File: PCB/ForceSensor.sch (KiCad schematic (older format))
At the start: 12 parts, among them J1 Conn_01x15, J2 Conn_01x15, J3 Conn_01x02, J4 Conn_01x01, J5 Conn_01x01, U1 MCP6004, U2 L7905

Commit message: New schematic
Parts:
- removed A1: Arduino_Nano_v3.x, Module:Arduino_Nano, symbol MCU_Module:Arduino_Nano_v3.x
- removed C1: C_Small, symbol Device:C_Small
- removed J1, J2: Conn_01x15, symbol Connector_Generic:Conn_01x15
- removed J3: Conn_01x02, symbol Connector_Generic:Conn_01x02
- removed J4, J5: Conn_01x01, symbol Connector_Generic:Conn_01x01
- removed R1, R2, R3: R, symbol Device:R
- removed U1: MCP6004, symbol Amplifier_Operational:MCP6004
- removed U2: L7905, symbol Regulator_Linear:L7905
- added C? (x6): C_Small, symbol Device:C_Small
- added J? (x2): Conn_01x10, symbol Connector_Generic:Conn_01x10
- added R? (x8): R_Small_US, symbol Device:R_Small_US
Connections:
- net labels removed: +3V, +5V, -5V, GND, VIN
- wire segments 36 -> 0
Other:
- note removed: "-5V regulator"
- note removed: "-Vref for sensors\n(Step down to 1V)"
- note removed: "Amplify Sensor Signal"
- note removed: "Connectors for Arduino"
- note removed: "Power from Battery to Arduino"
- note removed: "Power the OpAmps"
- note removed: "Sensor"
- note removed: "To sensors"

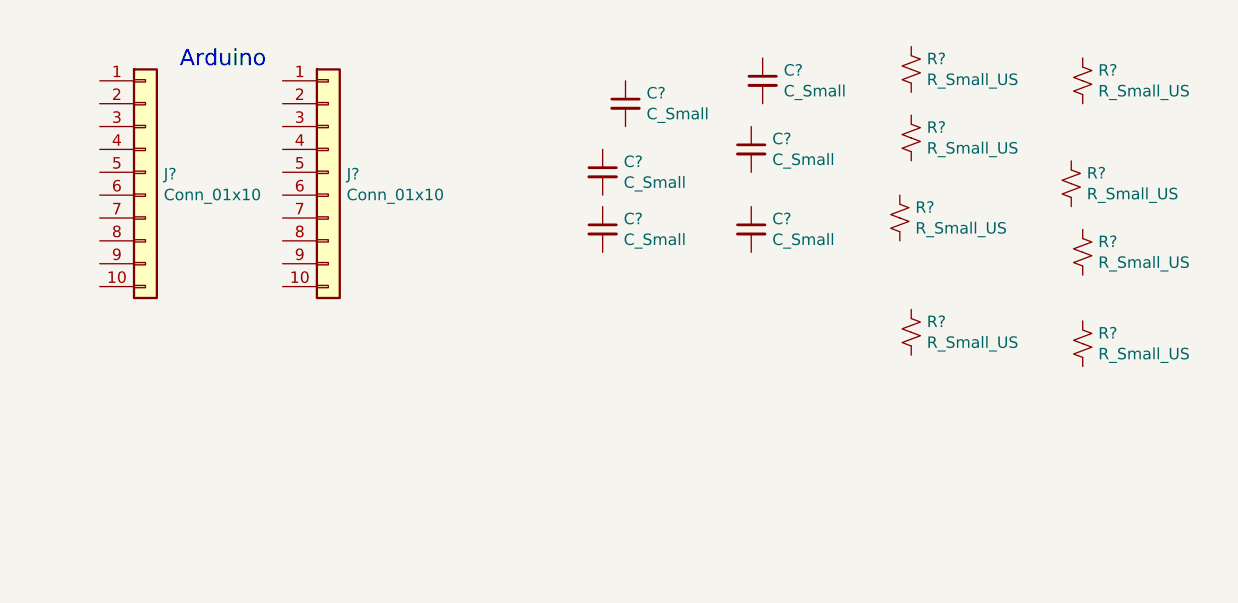
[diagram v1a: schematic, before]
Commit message: Added schematics for rfs pcb
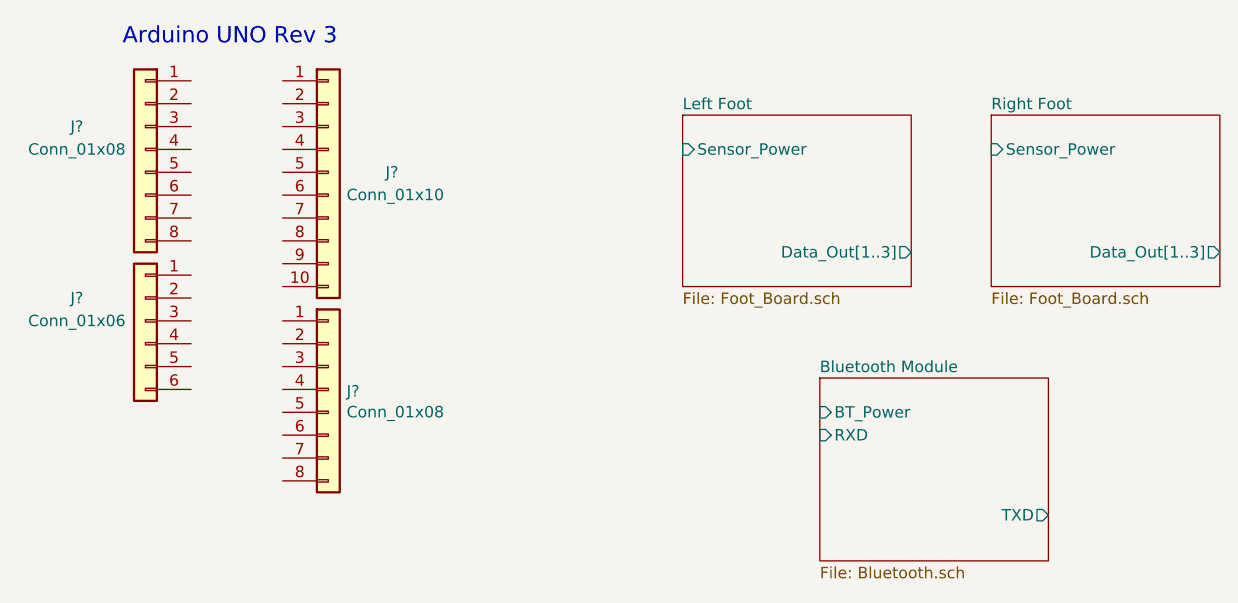
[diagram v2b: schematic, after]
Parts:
- removed C? (x6): C_Small, symbol Device:C_Small
- removed J?: Conn_01x10, symbol Connector_Generic:Conn_01x10
- removed R? (x8): R_Small_US, symbol Device:R_Small_US
- added J? (x2): Conn_01x08, symbol Connector_Generic:Conn_01x08
- added J?: Conn_01x06, symbol Connector_Generic:Conn_01x06
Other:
- note added: "Arduino UNO Rev 3"
- note removed: "Arduino"
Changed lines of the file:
@@
 $Descr A4 11693 8268
 encoding utf-8
-Sheet 1 1
+Sheet 1 4
 Title ""
 Date ""
@@
 $Comp
 L Connector_Generic:Conn_01x10 J?
-U 1 1 611AF6E7
-P 3050 3100
-F 0 "J?" H 3130 3092 50  0000 L CNN
-F 1 "Conn_01x10" H 3130 3001 50  0000 L CNN
-F 2 "" H 3050 3100 50  0001 C CNN
-F 3 "~" H 3050 3100 50  0001 C CNN
-	1    3050 3100
-	1    0    0    -1
-$EndComp
-$Comp
-L Connector_Generic:Conn_01x10 J?
 U 1 1 611AFD66
 P 3850 3100
-F 0 "J?" H 3930 3092 50  0000 L CNN
+F 0 "J?" H 4100 3100 50  0000 L CNN
 F 1 "Conn_01x10" H 3930 3001 50  0000 L CNN
 F 2 "" H 3850 3100 50  0001 C CNN
@@
 	1    0    0    -1
 $EndComp
-Text Notes 3200 2650 0    71   ~ 0
-Arduino
+Text Notes 2950 2550 0    71   ~ 0
+Arduino UNO Rev 3
+$Sheet
+S 5400 2850 1000 750
+U 611C8367
+F0 "Left Foot" 50
+F1 "Foot_Board.sch" 50
+F2 "Sensor_Power" I L 5400 3000 50
+F3 "Data_Out[1..3]" O R 6400 3450 50
+$EndSheet
+$Sheet
+S 6750 2850 1000 750
+U 611CB06B
+F0 "Right Foot" 50
+F1 "Foot_Board.sch" 50
+F2 "Sensor_Power" I L 6750 3000 50
+F3 "Data_Out[1..3]" O R 7750 3450 50
+$EndSheet
 $Comp
-L Device:C_Small C?
-U 1 1 611B1301
-P 5050 3100
-F 0 "C?" H 5142 3146 50  0000 L CNN
-F 1 "C_Small" H 5142 3055 50  0000 L CNN
-F 2 "" H 5050 3100 50  0001 C CNN
-F 3 "~" H 5050 3100 50  0001 C CNN
-	1    5050 3100
+L Connector_Generic:Conn_01x08 J?
+U 1 1 611E3554
+P 3850 4050
+F 0 "J?" H 3930 4042 50  0000 L CNN
+F 1 "Conn_01x08" H 3930 3951 50  0000 L CNN
+F 2 "" H 3850 4050 50  0001 C CNN
+F 3 "~" H 3850 4050 50  0001 C CNN
+	1    3850 4050
 	1    0    0    -1
 $EndComp
 $Comp
-L Device:C_Small C?
-U 1 1 611B18D9
-P 5700 3000
-F 0 "C?" H 5792 3046 50  0000 L CNN
-F 1 "C_Small" H 5792 2955 50  0000 L CNN
-F 2 "" H 5700 3000 50  0001 C CNN
-F 3 "~" H 5700 3000 50  0001 C CNN
-	1    5700 3000
-	1    0    0    -1
+L Connector_Generic:Conn_01x08 J?
+U 1 1 611E4224
+P 3050 3000
+F 0 "J?" H 3350 3100 50  0000 C CNN
+F 1 "Conn_01x08" H 3350 3000 50  0000 C CNN
+F 2 "" H 3050 3000 50  0001 C CNN
+F 3 "~" H 3050 3000 50  0001 C CNN
+	1    3050 3000
+	-1   0    0    -1
 $EndComp
 $Comp
-L Device:C_Small C?
-U 1 1 611B1E5F
-P 5150 2800
-F 0 "C?" H 5242 2846 50  0000 L CNN
-F 1 "C_Small" H 5242 2755 50  0000 L CNN
-F 2 "" H 5150 2800 50  0001 C CNN
-F 3 "~" H 5150 2800 50  0001 C CNN
-	1    5150 2800
-	1    0    0    -1
+L Connector_Generic:Conn_01x06 J?
+U 1 1 611E4D84
+P 3050 3750
+F 0 "J?" H 3350 3850 50  0000 C CNN
+F 1 "Conn_01x06" H 3350 3750 50  0000 C CNN
+F 2 "" H 3050 3750 50  0001 C CNN
+F 3 "~" H 3050 3750 50  0001 C CNN
+	1    3050 3750
+	-1   0    0    -1
 $EndComp
-$Comp
-L Device:C_Small C?
-U 1 1 611B356B
-P 5700 3350
-F 0 "C?" H 5792 3396 50  0000 L CNN
-F 1 "C_Small" H 5792 3305 50  0000 L CNN
-F 2 "" H 5700 3350 50  0001 C CNN
-F 3 "~" H 5700 3350 50  0001 C CNN
-	1    5700 3350
-	1    0    0    -1
-$EndComp
-$Comp
-L Device:C_Small C?
-U 1 1 611B391E
-P 5050 3350
-F 0 "C?" H 5142 3396 50  0000 L CNN
-F 1 "C_Small" H 5142 3305 50  0000 L CNN
-F 2 "" H 5050 3350 50  0001 C CNN
-F 3 "~" H 5050 3350 50  0001 C CNN
-	1    5050 3350
-	1    0    0    -1
-$EndComp
-$Comp
-L Device:C_Small C?
-U 1 1 611B4706
-P 5750 2700
-F 0 "C?" H 5842 2746 50  0000 L CNN
-F 1 "C_Small" H 5842 2655 50  0000 L CNN
-F 2 "" H 5750 2700 50  0001 C CNN
-F 3 "~" H 5750 2700 50  0001 C CNN
-	1    5750 2700
-	1    0    0    -1
-$EndComp
-$Comp
-L Device:R_Small_US R?
-U 1 1 611B4D3E
-P 6400 2650
-F 0 "R?" H 6468 2696 50  0000 L CNN
-F 1 "R_Small_US" H 6468 2605 50  0000 L CNN
-F 2 "" H 6400 2650 50  0001 C CNN
-F 3 "~" H 6400 2650 50  0001 C CNN
-	1    6400 2650
-	1    0    0    -1
-$EndComp
-$Comp
-L Device:R_Small_US R?
-U 1 1 611B541B
-P 6400 2950
-F 0 "R?" H 6468 2996 50  0000 L CNN
-F 1 "R_Small_US" H 6468 2905 50  0000 L CNN
-F 2 "" H 6400 2950 50  0001 C CNN
-F 3 "~" H 6400 2950 50  0001 C CNN
-	1    6400 2950
-	1    0    0    -1
-$EndComp
-$Comp
-L Device:R_Small_US R?
-U 1 1 611B565A
-P 6350 3300
-F 0 "R?" H 6418 3346 50  0000 L CNN
-F 1 "R_Small_US" H 6418 3255 50  0000 L CNN
-F 2 "" H 6350 3300 50  0001 C CNN
-F 3 "~" H 6350 3300 50  0001 C CNN
-	1    6350 3300
-	1    0    0    -1
-$EndComp
-$Comp
-L Device:R_Small_US R?
-U 1 1 611B59E7
-P 7150 2700
-F 0 "R?" H 7218 2746 50  0000 L CNN
-F 1 "R_Small_US" H 7218 2655 50  0000 L CNN
-F 2 "" H 7150 2700 50  0001 C CNN
-F 3 "~" H 7150 2700 50  0001 C CNN
-	1    7150 2700
-	1    0    0    -1
-$EndComp
-$Comp
-L Device:R_Small_US R?
-U 1 1 611B5C51
-P 7100 3150
-F 0 "R?" H 7168 3196 50  0000 L CNN
-F 1 "R_Small_US" H 7168 3105 50  0000 L CNN
-F 2 "" H 7100 3150 50  0001 C CNN
-F 3 "~" H 7100 3150 50  0001 C CNN
-	1    7100 3150
-	1    0    0    -1
-$EndComp
-$Comp
-L Device:R_Small_US R?
-U 1 1 611B5DE3
-P 7150 3450
-F 0 "R?" H 7218 3496 50  0000 L CNN
-F 1 "R_Small_US" H 7218 3405 50  0000 L CNN
-F 2 "" H 7150 3450 50  0001 C CNN
-F 3 "~" H 7150 3450 50  0001 C CNN
-	1    7150 3450
-	1    0    0    -1
-$EndComp
-$Comp
-L Device:R_Small_US R?
-U 1 1 611B8589
-P 6400 3800
-F 0 "R?" H 6468 3846 50  0000 L CNN
-F 1 "R_Small_US" H 6468 3755 50  0000 L CNN
-F 2 "" H 6400 3800 50  0001 C CNN
-F 3 "~" H 6400 3800 50  0001 C CNN
-	1    6400 3800
-	1    0    0    -1
-$EndComp
-$Comp
-L Device:R_Small_US R?
-U 1 1 611B859B
-P 7150 3850
-F 0 "R?" H 7218 3896 50  0000 L CNN
-F 1 "R_Small_US" H 7218 3805 50  0000 L CNN
-F 2 "" H 7150 3850 50  0001 C CNN
-F 3 "~" H 7150 3850 50  0001 C CNN
-	1    7150 3850
-	1    0    0    -1
-$EndComp
+$Sheet
+S 6000 4000 1000 800
+U 611E7D97
+F0 "Bluetooth Module" 50
+F1 "Bluetooth.sch" 50
+F2 "BT_Power" I L 6000 4150 50
+F3 "TXD" O R 7000 4600 50
+F4 "RXD" I L 6000 4250 50
+$EndSheet
 $EndSCHEMATC

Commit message: Finished schematic
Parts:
- added J?: Conn_01x04, symbol Connector_Generic:Conn_01x04
- added J?: Conn_01x02, symbol Connector_Generic:Conn_01x02
- added R?: 10K Ohm, symbol Device:R_Small_US
- added R?: 560 Ohm, symbol Device:R_Small_US
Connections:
- net GND: now reaches J?.4 (Pin_4)
- net GND: now also J?.6 (Pin_6), J?.7 (Pin_7), J?.2 (Pin_2), J?.2 (Pin_2), R?.1
- net D3: now reaches J?.5 (Pin_5)
- net D3: now also R?.2
- net D2: now reaches J?.6 (Pin_6)
- net D2: now also J?.3 (Pin_3)
- net +3V3: now reaches J?.4 (Pin_4)
- net +5V: now reaches J?.5 (Pin_5)
- net +5V: now also J?.1 (Pin_1)
- net VIN: now reaches J?.8 (Pin_8)
- net VIN: now also J?.1 (Pin_1)
- net Left_Data1: now reaches J?.1 (Pin_1)
- net Left_Data2: now reaches J?.2 (Pin_2)
- net Left_Data3: now reaches J?.3 (Pin_3)
- net Right_Data1: now reaches J?.4 (Pin_4)
- net Right_Data2: now reaches J?.5 (Pin_5)
- net Right_Data3: now reaches J?.6 (Pin_6)
- new net: J?.4 (Pin_4), R?.1, R?.2
- no-connect marks 0 -> 18
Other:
- note added: "*D10"
- note added: "*D11"
- note added: "*D3"
- note added: "*D5"
- note added: "*D6"
- note added: "*D9"
- note added: "+3V3"
- note added: "+5V"
- note added: "A0"
- note added: "A1"
- note added: "A2"
- note added: "A3"
- note added: "A4"
- note added: "A5"
- note added: "AREF"
- note added: "Arduino UNO Rev 3\n * PWM"
- note added: "D0/RX"
- note added: "D1/TX"
- note added: "D12"
- note added: "D13"
- note added: "D2"
- note added: "D4"
- note added: "D7"
- note added: "D8"
- note added: "GND"
- note added: "IOREF"
- note added: "NC"
- note added: "RESET"
- note added: "SCL"
- note added: "SDA"
- note added: "VIN"
- note removed: "Arduino UNO Rev 3"
- moved on the sheet: J?

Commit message: Small changes to schematic
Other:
- note added: "HC-06 BT Connection"
- note added: "Left and Right Foot Sensor Inputs"
- moved on the sheet: J?, R?
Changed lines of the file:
@@
 Arduino UNO Rev 3\n       * PWM
 $Sheet
-S 5400 2850 1000 750
+S 6850 2200 1000 750
 U 611C8367
 F0 "Left Foot" 50
 F1 "Foot_Board.sch" 50
-F2 "Sensor_Power" I L 5400 3000 50
-F3 "Data_Out[1..3]" O R 6400 3450 50
+F2 "Sensor_Power" I L 6850 2350 50
+F3 "Data_Out[1..3]" O R 7850 2800 50
 $EndSheet
 $Sheet
-S 5400 1800 1000 750
+S 8700 2200 1000 750
 U 611CB06B
 F0 "Right Foot" 50
 F1 "Foot_Board.sch" 50
-F2 "Sensor_Power" I L 5400 1950 50
-F3 "Data_Out[1..3]" O R 6400 2400 50
+F2 "Sensor_Power" I L 8700 2350 50
+F3 "Data_Out[1..3]" O R 9700 2800 50
 $EndSheet
 $Comp
@@
 L Connector_Generic:Conn_01x04 J?
 U 1 1 611DBB38
-P 5300 4550
+P 4900 4350
 AR Path="/611E7D97/611DBB38" Ref="J?"  Part="1"
 AR Path="/611DBB38" Ref="J?"  Part="1"
-F 0 "J?" H 5300 4850 50  0000 C CNN
-F 1 "Conn_01x04" H 5350 4750 50  0000 C CNN
-F 2 "" H 5300 4550 50  0001 C CNN
-F 3 "~" H 5300 4550 50  0001 C CNN
-	1    5300 4550
+F 0 "J?" H 4900 4650 50  0000 C CNN
+F 1 "Conn_01x04" H 4950 4550 50  0000 C CNN
+F 2 "" H 4900 4350 50  0001 C CNN
+F 3 "~" H 4900 4350 50  0001 C CNN
+	1    4900 4350
 	-1   0    0    -1
 $EndComp
@@
 L BPSDisplay:GND #PWR?
 U 1 1 611DBB3F
-P 6700 4550
+P 6300 4350
 AR Path="/611E7D97/611DBB3F" Ref="#PWR?"  Part="1"
 AR Path="/611DBB3F" Ref="#PWR?"  Part="1"
-F 0 "#PWR?" H 6700 4300 50  0001 C CNN
-F 1 "GND" V 6705 4422 50  0000 R CNN
-F 2 "" H 6700 4550 50  0000 C CNN
-F 3 "" H 6700 4550 50  0000 C CNN
-	1    6700 4550
+F 0 "#PWR?" H 6300 4100 50  0001 C CNN
+F 1 "GND" V 6305 4222 50  0000 R CNN
+F 2 "" H 6300 4350 50  0000 C CNN
+F 3 "" H 6300 4350 50  0000 C CNN
+	1    6300 4350
 	0    -1   -1   0
 $EndComp
@@
 L Device:R_Small_US R?
 U 1 1 611DBB45
-P 6100 4650
+P 5700 4450
 AR Path="/611E7D97/611DBB45" Ref="R?"  Part="1"
 AR Path="/611DBB45" Ref="R?"  Part="1"
-F 0 "R?" H 6168 4696 50  0000 L CNN
-F 1 "10K Ohm" H 6168 4605 50  0000 L CNN
-F 2 "" H 6100 4650 50  0001 C CNN
-F 3 "~" H 6100 4650 50  0001 C CNN
-	1    6100 4650
+F 0 "R?" H 5768 4496 50  0000 L CNN
+F 1 "10K Ohm" H 5768 4405 50  0000 L CNN
+F 2 "" H 5700 4450 50  0001 C CNN
+F 3 "~" H 5700 4450 50  0001 C CNN
+	1    5700 4450
 	1    0    0    -1
 $EndComp
@@
 L Device:R_Small_US R?
 U 1 1 611DBB4B
-P 6100 4850
+P 5700 4650
 AR Path="/611E7D97/611DBB4B" Ref="R?"  Part="1"
 AR Path="/611DBB4B" Ref="R?"  Part="1"
-F 0 "R?" H 6168 4896 50  0000 L CNN
-F 1 "560 Ohm" H 6168 4805 50  0000 L CNN
-F 2 "" H 6100 4850 50  0001 C CNN
-F 3 "~" H 6100 4850 50  0001 C CNN
-	1    6100 4850
-	1    0    0    -1
-$EndComp
-Wire Wire Line
-	5500 4650 5700 4650
-Wire Wire Line
-	5500 4550 6100 4550
-Wire Wire Line
-	5500 4750 6100 4750
-Wire Wire Line
-	6700 4550 6100 4550
-Connection ~ 6100 4550
-Connection ~ 6100 4750
-Wire Wire Line
-	6100 4950 6700 4950
-Wire Wire Line
-	5700 4450 5500 4450
-Wire Notes Line
-	4600 4850 4600 2200
+F 0 "R?" H 5768 4696 50  0000 L CNN
+F 1 "560 Ohm" H 5768 4605 50  0000 L CNN
+F 2 "" H 5700 4650 50  0001 C CNN
+F 3 "~" H 5700 4650 50  0001 C CNN
+	1    5700 4650
+	1    0    0    -1
+$EndComp
+Wire Wire Line
+	5100 4450 5300 4450
+Wire Wire Line
+	5100 4350 5700 4350
+Wire Wire Line
+	5100 4550 5700 4550
+Wire Wire Line
+	6300 4350 5700 4350
+Connection ~ 5700 4350
+Connection ~ 5700 4550
+Wire Wire Line
+	5700 4750 6300 4750
+Wire Wire Line
+	5300 4250 5100 4250
 $Comp
 L power:+3V3 #PWR?
@@
 L power:+5V #PWR?
 U 1 1 611ED85A
-P 5700 4450
-F 0 "#PWR?" H 5700 4300 50  0001 C CNN
-F 1 "+5V" H 5715 4623 50  0000 C CNN
-F 2 "" H 5700 4450 50  0001 C CNN
-F 3 "" H 5700 4450 50  0001 C CNN
-	1    5700 4450
-	1    0    0    -1
-$EndComp
-Text Label 6700 4950 0    50   ~ 0
+P 5300 4250
+F 0 "#PWR?" H 5300 4100 50  0001 C CNN
+F 1 "+5V" H 5315 4423 50  0000 C CNN
+F 2 "" H 5300 4250 50  0001 C CNN
+F 3 "" H 5300 4250 50  0001 C CNN
+	1    5300 4250
+	1    0    0    -1
+$EndComp
+Text Label 6300 4750 0    50   ~ 0
 D3
-Text Label 5700 4650 0    50   ~ 0
+Text Label 5300 4450 0    50   ~ 0
 D2
 $Comp
@@
 L power:+5V #PWR?
 U 1 1 611F02A4
-P 5200 2950
-F 0 "#PWR?" H 5200 2800 50  0001 C CNN
-F 1 "+5V" H 5215 3123 50  0000 C CNN
-F 2 "" H 5200 2950 50  0001 C CNN
-F 3 "" H 5200 2950 50  0001 C CNN
-	1    5200 2950
+P 6650 2300
+F 0 "#PWR?" H 6650 2150 50  0001 C CNN
+F 1 "+5V" H 6665 2473 50  0000 C CNN
+F 2 "" H 6650 2300 50  0001 C CNN
+F 3 "" H 6650 2300 50  0001 C CNN
+	1    6650 2300
 	1    0    0    -1
 $EndComp
@@
 L power:+5V #PWR?
 U 1 1 611F08C5
-P 5250 1900
-F 0 "#PWR?" H 5250 1750 50  0001 C CNN
-F 1 "+5V" H 5265 2073 50  0000 C CNN
-F 2 "" H 5250 1900 50  0001 C CNN
-F 3 "" H 5250 1900 50  0001 C CNN
-	1    5250 1900
-	1    0    0    -1
-$EndComp
-Wire Wire Line
-	5200 2950 5200 3000
-Wire Wire Line
-	5200 3000 5400 3000
-Wire Wire Line
-	5250 1900 5250 1950
-Wire Wire Line
-	5250 1950 5400 1950
+P 8550 2300
+F 0 "#PWR?" H 8550 2150 50  0001 C CNN
+F 1 "+5V" H 8565 2473 50  0000 C CNN
+F 2 "" H 8550 2300 50  0001 C CNN
+F 3 "" H 8550 2300 50  0001 C CNN
+	1    8550 2300
+	1    0    0    -1
+$EndComp
+Wire Wire Line
+	6650 2300 6650 2350
+Wire Wire Line
+	6650 2350 6850 2350
+Wire Wire Line
+	8550 2300 8550 2350
+Wire Wire Line
+	8550 2350 8700 2350
 Wire Notes Line
 	2050 4850 2050 2200
-Wire Notes Line
-	2050 4850 4600 4850
 Wire Notes Line
 	2050 2200 4600 2200
 Wire Bus Line
-	6400 3450 6500 3450
+	7850 2800 7950 2800
 Wire Bus Line
-	6400 2400 6500 2400
-Text Label 6500 2400 0    50   ~ 0
+	9700 2800 9800 2800
+Text Label 9800 2800 0    50   ~ 0
 Right_Data[1..3]
-Text Label 6500 3450 0    50   ~ 0
+Text Label 7950 2800 0    50   ~ 0
 Left_Data[1..3]
 Text Label 2700 3550 2    50   ~ 0
@@
 Wire Wire Line
 	2850 3550 2700 3550
+Text Notes 5100 3950 0    71   ~ 0
+HC-06 BT Connection
+Wire Notes Line
+	4600 3750 6650 3750
+Wire Notes Line
+	6650 3750 6650 4850
+Wire Notes Line
+	4600 2200 4600 4850
+Wire Notes Line
+	2050 4850 6650 4850
+Wire Notes Line
+	6500 1700 10500 1700
+Wire Notes Line
+	6500 3150 10500 3150
+Text Notes 7550 1900 0    71   ~ 0
+Left and Right Foot Sensor Inputs
+Wire Notes Line
+	6500 1700 6500 3150
+Wire Notes Line
+	10500 1700 10500 3150
 $EndSCHEMATC
